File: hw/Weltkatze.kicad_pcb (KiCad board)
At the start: 6 copper layers, 58.7 x 58.7 mm, 108 parts, among them J1 USB_C_Receptacle_USB2.0_14P, J2 CONN_BAT, J4 LED_OUT, J6 UART, J7 ESP_PWR, SW2 SW_Push, SW3 SW_Push, U1 TPS3700DDCR, U2 TP4056, U3 TPS61023DRLR, U5 TPS2111APW, U6 SPX3819M5-L-3-3, U7 BMP280, U8 LSM303C, U9 ESP32-C6-MINI-1/U, Y1 32.768k

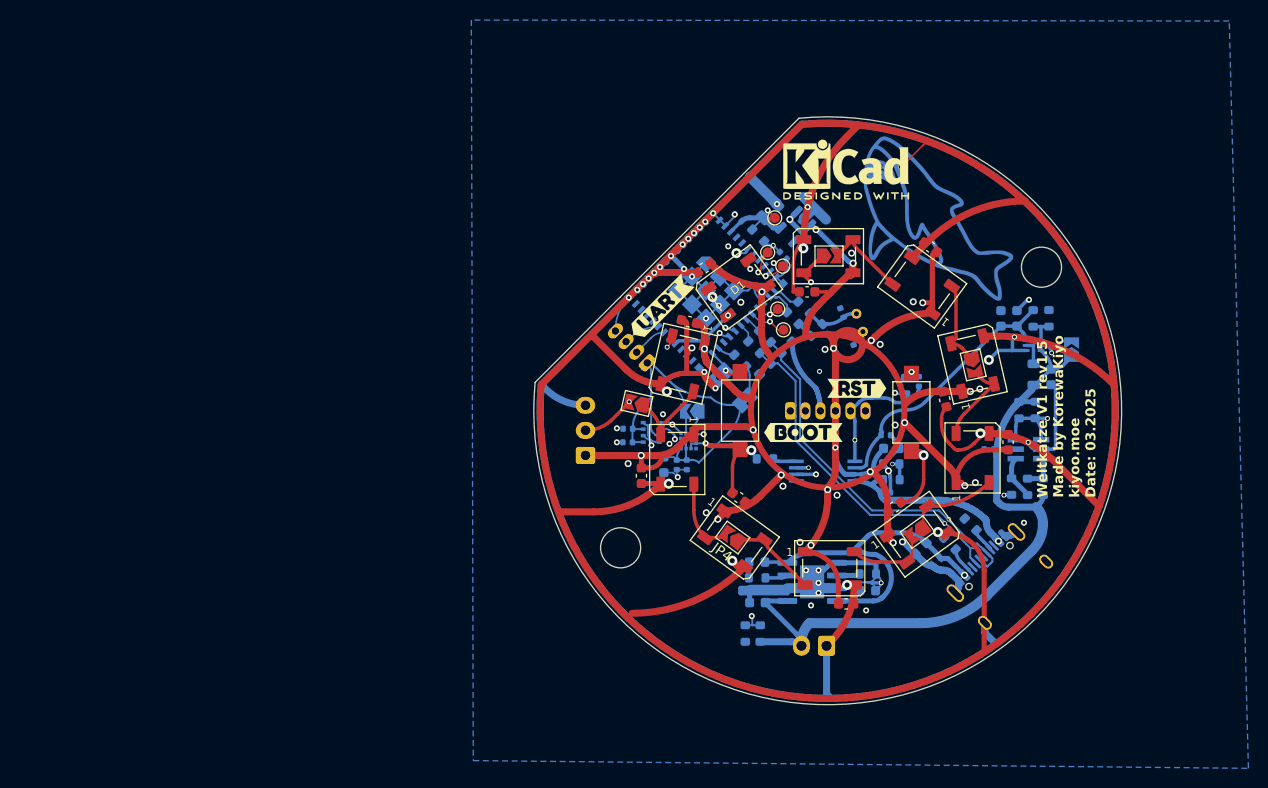
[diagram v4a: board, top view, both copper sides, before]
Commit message: Redesign work
I'm going towards a single-sided minimum viable design, so that I only need to place and hotplate one side to  verify function, before adding things like battery and USB by hand.
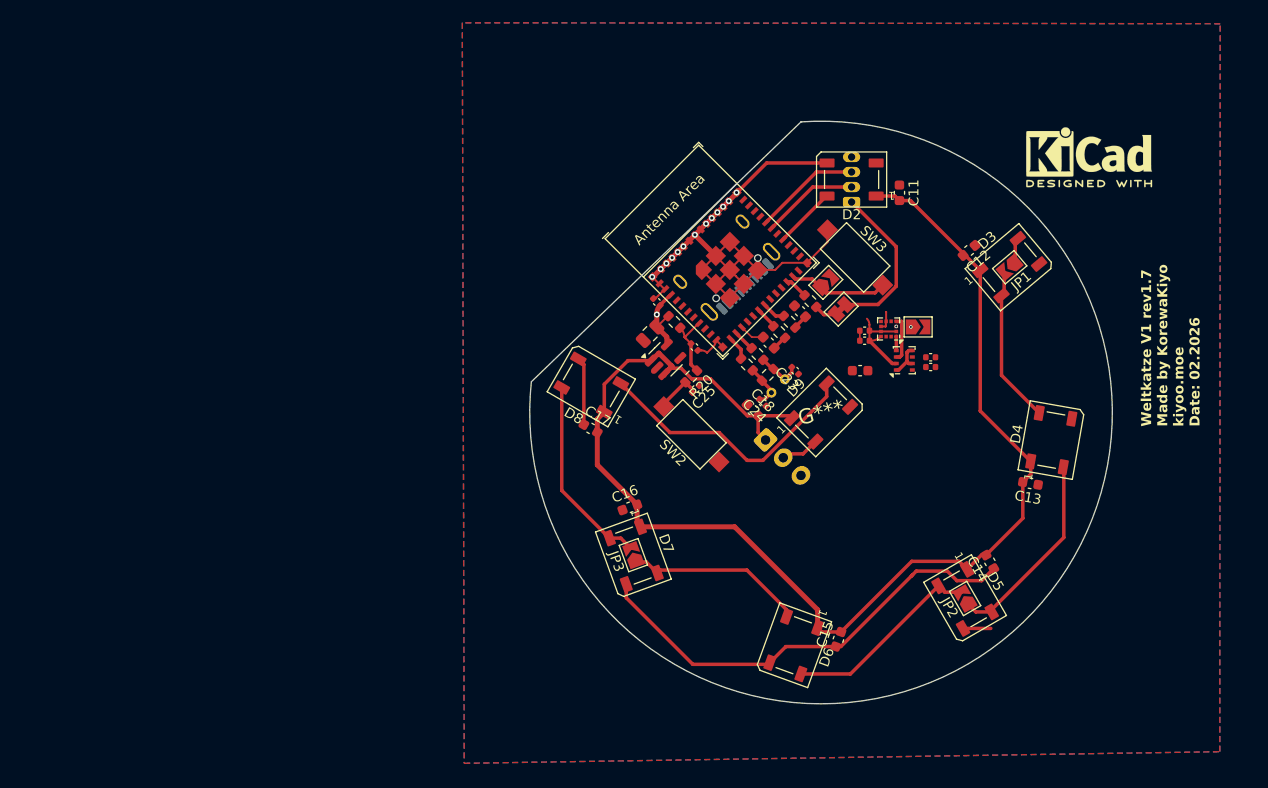
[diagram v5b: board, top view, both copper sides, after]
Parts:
- removed C1, C10, C19, C2, C20, C3, C5, C6, C7: 10u, Capacitor_SMD:C_0603_1608Metric
- removed C4, C8, C9: 0.1u, Capacitor_SMD:C_0402_1005Metric
- removed CR1: ESDA25P35-1U1M, lib:QFN1610_STM-M
- removed D1: R, LED_SMD:LED_0603_1608Metric
- removed D10, D11: WS2812B, LED_SMD:LED_WS2812B_PLCC4_5.0x5.0mm_P3.2mm
- removed the G*** at (151.2, 67.5)
- removed J2: CONN_BAT, Connector_JST:JST_XH_B2B-XH-A_1x02_P2.50mm_Vertical
- removed J7: ESP_PWR, Connector_JST:JST_ZH_B6B-ZR_1x06_P1.50mm_Vertical
- removed JP4, JP5: SolderJumper_2_Open, Jumper:SolderJumper-2_P1.3mm_Open_TrianglePad1.0x1.5mm
- removed L1: 470n, Inductor_SMD:L_0805_2012Metric
- removed R1, R2: 5.1k, Resistor_SMD:R_0603_1608Metric
- removed R10: 100k, Resistor_SMD:R_0603_1608Metric
- removed R11: 732k, Resistor_SMD:R_0603_1608Metric
- removed R12, R8: 1k, Resistor_SMD:R_0603_1608Metric
- removed R13: 470, Resistor_SMD:R_0603_1608Metric
- removed R14: 191, Resistor_SMD:R_0603_1608Metric
- removed R15, R16: 200k, Resistor_SMD:R_0603_1608Metric
- removed R3: 597k, Resistor_SMD:R_0603_1608Metric
- removed R4, R5, R6: 49.9k, Resistor_SMD:R_0603_1608Metric
- removed R7: 66.5k, Resistor_SMD:R_0603_1608Metric
- removed R9: 1.5k, Resistor_SMD:R_0603_1608Metric
- removed the REF** at (169.0, 85.7)
- removed TP1: MTMS, TestPoint:TestPoint_Pad_D1.0mm
- removed TP2: MTDI, TestPoint:TestPoint_Pad_D1.0mm
- removed TP3: MTCK, TestPoint:TestPoint_Pad_D1.0mm
- removed TP4: MTDO, TestPoint:TestPoint_Pad_D1.0mm
- removed TP5: 3V3, TestPoint:TestPoint_Pad_D1.0mm
- removed U1: TPS3700DDCR, lib:DDC6_TEX-M
- removed U2: TP4056, lib:SOP127P600X175-9N
- removed U3: TPS61023DRLR, lib:DRL0006A
- removed U5: TPS2111APW, lib:PW8
- removed kibuzzard-67C8587C: G***, kibuzzard-67C8587C
- removed kibuzzard-67C8594C: G***, kibuzzard-67C8594C
- removed kibuzzard-67C8753B: G***, kibuzzard-67C8753B
- C23, C24, C25, C26, C27, C28, C29, C30, C31, C32, C33, C34, C35, JP6, JP7, JP9, R17, R18, R19, R20, R21, R22, R23, R24, U6, U7, U8, U9: moved to F.Cu
- moved G*** 66.4 mm to (144.0, 92.0), turned to 15 degrees
- moved kibuzzard-67CB1547 46.5 mm to (152.2, 69.2)
- moved J1 43.4 mm to (133.8, 76.7), turned to 44 degrees
- moved C35 31.2 mm to (154.9, 87.5), turned to 0 degrees
- moved C34 31.0 mm to (154.9, 86.5), turned to 0 degrees
- moved C17 30.9 mm to (121.0, 93.6), turned to -30 degrees
- moved D8 30.0 mm to (121.1, 89.3), turned to 150 degrees
- moved JP3 28.4 mm to (125.3, 106.2), turned to 110 degrees
- moved D7 28.4 mm to (125.3, 106.3), turned to -70 degrees
- moved kibuzzard-67CB17AB 26.5 mm to (147.1, 102.9), turned to 135 degrees
- moved C16 26.4 mm to (124.9, 101.5), turned to 20 degrees
- moved U7 26.3 mm to (152.3, 86.8)
- moved C15 26.0 mm to (145.7, 114.6), turned to 70 degrees
- moved J6 25.9 mm to (147.1, 71.0), turned to 90 degrees
- moved D6 25.8 mm to (141.3, 115.2), turned to -110 degrees
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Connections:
- net Net-(U9-GPIO12/USB_D-) renamed /Logic/USB_N
- net Net-(U9-GPIO13/USB_D+) renamed /Logic/USB_P
- D9 pad 2: Net-(D10-DIN) -> Net-(D9-DOUT)
- J4 pad 2: Net-(D11-DOUT) -> Net-(D9-DOUT)
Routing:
- net GND: track 426.0 -> 129.9 mm, vias 74 -> 13
- net VBAT: track 74.2 -> 0.00 mm
- net /Power/USB_VBUS: track 53.3 -> 0.00 mm, vias 2 -> 0
- net /Logic/VBAT_MON: track 53.2 -> 0.00 mm, vias 2 -> 0
- net +3V3: track 80.2 -> 33.5 mm
- net /Logic/USBD_P: track 37.7 -> 1.52 mm, vias 1 -> 0
- net /Logic/USBD_N: track 37.4 -> 1.57 mm, vias 1 -> 0
- net +5V: track 164.2 -> 132.5 mm, vias 22 -> 0
- net /Power/VBUS: track 27.2 -> 0.00 mm
- net Net-(D8-DOUT): track 8.22 -> 27.9 mm
- net /Logic/ESP_RST: track 24.8 -> 6.85 mm, vias 2 -> 0
- net /Power/VBAT_EN: track 17.9 -> 0.00 mm, vias 2 -> 0
- net /Logic/ESP_SCL: track 16.2 -> 1.40 mm, vias 2 -> 0
- net Net-(D11-DOUT): track 14.7 -> 0.00 mm, vias 2 -> 0
- net /Logic/ESP_SDA: track 18.6 -> 4.65 mm, vias 3 -> 0
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- added copper zone on In1.Cu, net +5V
- added copper zone on In3.Cu, net +5V
- added copper zone on In4.Cu, net +5V
- added copper zone on F.Cu, net GND
- removed copper zone on In2.Cu, net +5V
- removed copper zone on In1.Cu, net GND
- removed copper zone on In3.Cu, net GND
- removed copper zone on In4.Cu, net GND
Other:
- board size 58.7 x 58.7 mm -> 58.1 x 58.1 mm
- board text added: "Weltkatze V1 rev1.7 Made by KorewaKiyo kiyoo.moe Date: 02.2026"
- board text removed: "Weltkatze V1 rev1.5 Made by KorewaKiyo kiyoo.moe Date: 03.2025"
